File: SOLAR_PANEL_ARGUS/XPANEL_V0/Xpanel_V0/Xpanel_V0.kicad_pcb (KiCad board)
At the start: 2 copper layers, 82.6 x 98 mm, 45 parts, among them J1 0530470810, Q1 BSS138, Q2 BSS138, Q3 MBT2222ADW1T1, Q4 BSS138, Q5 BSS138, Q6 MBT2222ADW1T1, U1 DRV8830DGQ

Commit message: changes made
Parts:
- moved D7 34.4 mm to (151.2, 99.3), turned to 180 degrees
- moved J1 32.5 mm to (145.4, 99.7)
- moved R14 30.8 mm to (168.1, 96.7)
- moved Q2 30.8 mm to (173.0, 83.9)
- moved C1 30.8 mm to (157.5, 96.8)
- moved C2 30.8 mm to (157.5, 98.7)
- moved C3 30.8 mm to (173.0, 81.0)
- moved C4 30.8 mm to (164.5, 102.6)
- moved Q5 30.8 mm to (164.3, 100.0)
- moved R11 30.8 mm to (172.2, 87.3)
- moved R15 30.8 mm to (171.8, 97.1)
- moved R16 30.8 mm to (171.9, 95.5)
- moved R18 30.8 mm to (164.7, 97.5)
- moved R3 30.8 mm to (151.4, 109.5)
- moved R4 30.8 mm to (151.4, 111.4)
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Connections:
- net /torque-coil renamed /coils
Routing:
- net /coils: track 0.00 -> 12329.7 mm, vias 0 -> 2
- net Net-(D7-K): track 0.00 -> 42.8 mm
- net SDA: track 0.00 -> 36.6 mm
- net SCL: track 0.00 -> 32.6 mm
- net SDA1_b4iso: track 0.00 -> 9.49 mm
- net Net-(Q5-G): track 0.00 -> 8.85 mm
- net Net-(Q1-S): track 0.00 -> 8.71 mm
- net Net-(U1-A0): track 0.00 -> 8.23 mm
- net Net-(Q1-G): track 0.00 -> 7.80 mm
- net Net-(Q4-G): track 0.00 -> 7.45 mm
- net Net-(Q4-S): track 0.00 -> 6.47 mm
- net +3.3V: track 0.00 -> 5.37 mm
- net VBATT: track 0.00 -> 4.95 mm
- net SCL1_b4iso: track 0.00 -> 4.56 mm
- net GND: track 0.00 -> 4.43 mm
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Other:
- outline, holes or cut-outs redrawn
- copper layers 2 -> 8

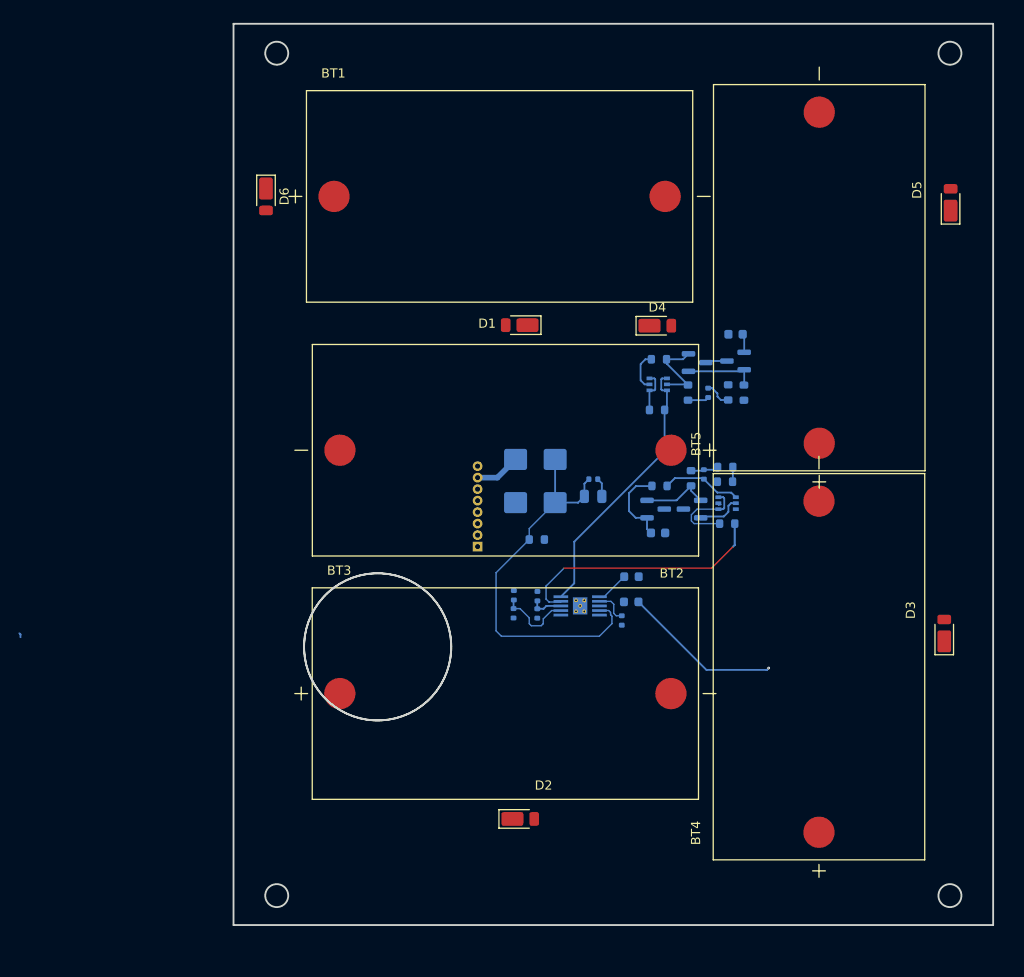
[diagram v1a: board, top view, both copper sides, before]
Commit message: need to add solar panel and solar sensor
added all coils and routed the planes.
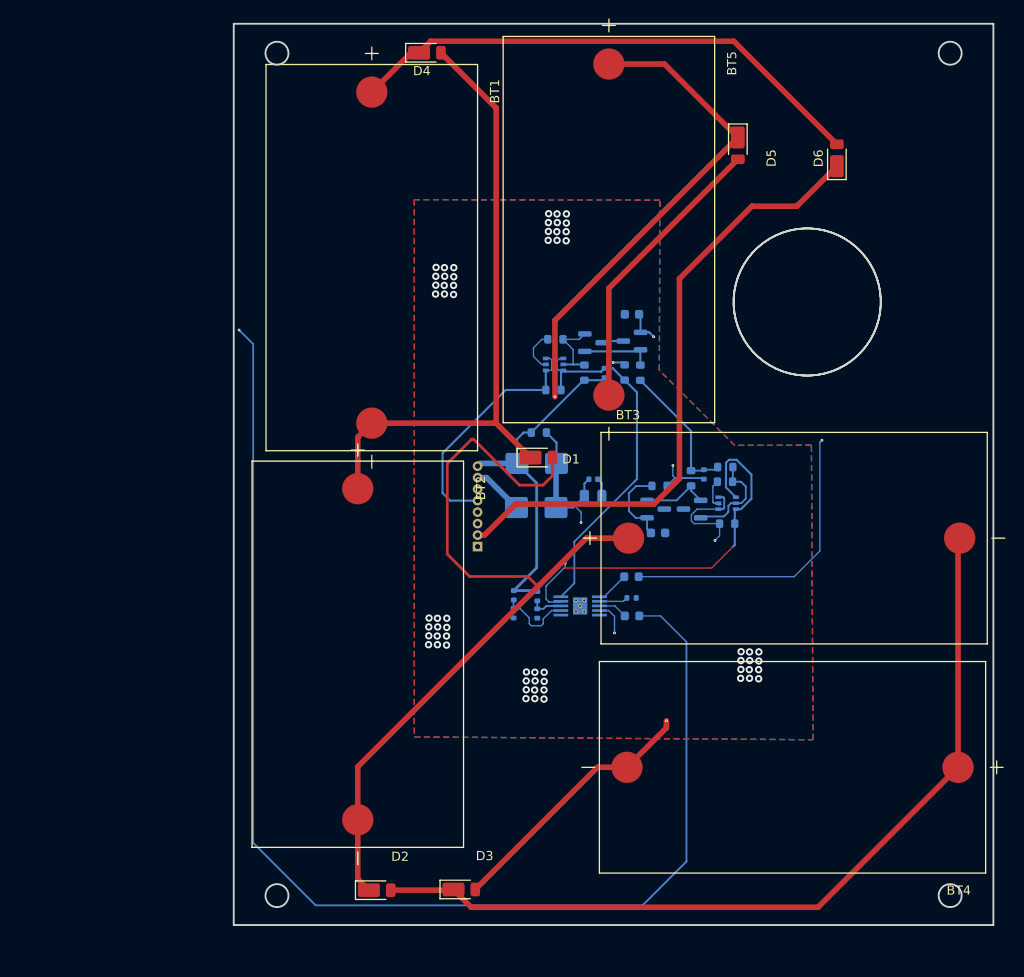
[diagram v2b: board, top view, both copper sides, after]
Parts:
- moved D6 62.2 mm to (184.0, 61.9), turned to 90 degrees
- moved D3 59.4 mm to (143.2, 141.4), turned to 0 degrees
- moved D4 38.8 mm to (139.4, 50.4)
- moved BT3 35.7 mm to (179.3, 103.2)
- moved BT2 27.4 mm to (131.9, 115.8), turned to -90 degrees
- moved D5 24.0 mm to (173.2, 60.5), turned to -90 degrees
- moved BT5 23.5 mm to (159.2, 69.6), turned to -90 degrees
- moved D2 17.4 mm to (134.0, 141.5)
- moved BT1 15.4 mm to (133.4, 72.7), turned to -90 degrees
- moved D1 14.5 mm to (151.5, 94.4), turned to 0 degrees
- moved R6 11.6 mm to (151.6, 91.7), turned to 0 degrees
- moved Q2 11.5 mm to (161.7, 81.8)
- moved C3 11.5 mm to (161.7, 78.9)
- moved Q1 11.5 mm to (157.5, 81.9)
- moved R11 11.5 mm to (160.9, 85.2)
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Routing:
- net /coils: track 12329.7 -> 80669.2 mm, vias 2 -> 9
- net Net-(D3-A): track 0.00 -> 122.8 mm, vias 0 -> 2
- net Net-(D2-A): track 0.00 -> 93.8 mm
- net Net-(D1-A): track 0.00 -> 91.8 mm
- net Net-(D1-K): track 0.00 -> 69.3 mm
- net /VSOLAR: track 0.00 -> 68.4 mm
- net Net-(D4-K): track 0.00 -> 57.5 mm
- net +3.3V: track 5.37 -> 52.9 mm
- net SDA: track 36.6 -> 68.9 mm, vias 0 -> 2
- net GND: track 4.43 -> 35.9 mm, vias 0 -> 60
- net SDA1_b4iso: track 9.49 -> 38.6 mm, vias 0 -> 2
- net SCL1_b4iso: track 4.56 -> 27.1 mm
- net Net-(D7-K): track 42.8 -> 33.6 mm, vias 0 -> 2
- net Net-(Q2-G): track 2.03 -> 10.7 mm, vias 0 -> 2
- net SCL: track 32.6 -> 39.6 mm
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- added copper zone on B.Cu, net GND
- added copper zone on F.Cu, net GND
- added copper zone on In1.Cu, net GND
- added copper zone on In2.Cu, net GND
- added copper zone on In3.Cu, net GND
- added copper zone on In4.Cu, net GND
- added copper zone on In5.Cu, net GND
- added copper zone on In6.Cu, net GND
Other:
- outline, holes or cut-outs redrawn
